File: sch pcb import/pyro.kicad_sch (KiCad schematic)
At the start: 34 parts, among them J601 Screw_01x02, J602 Screw_01x02, Q601 SISA12ADN, Q602 SISA12ADN, U601 LM358, U602 LM358

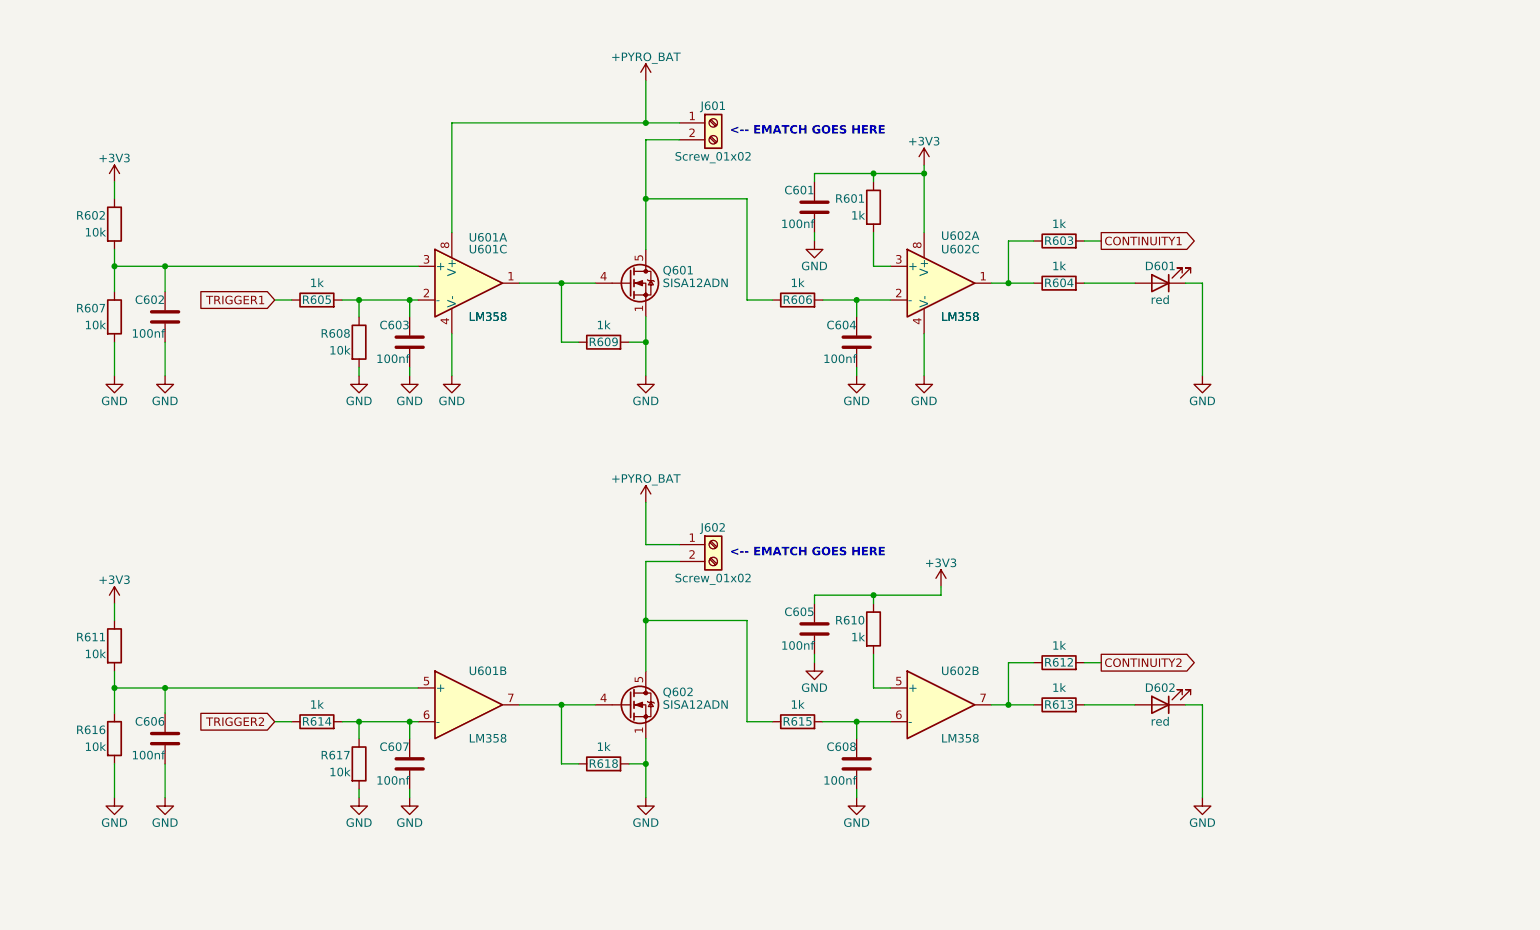
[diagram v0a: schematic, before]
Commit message: added servo and finished esp32 connections
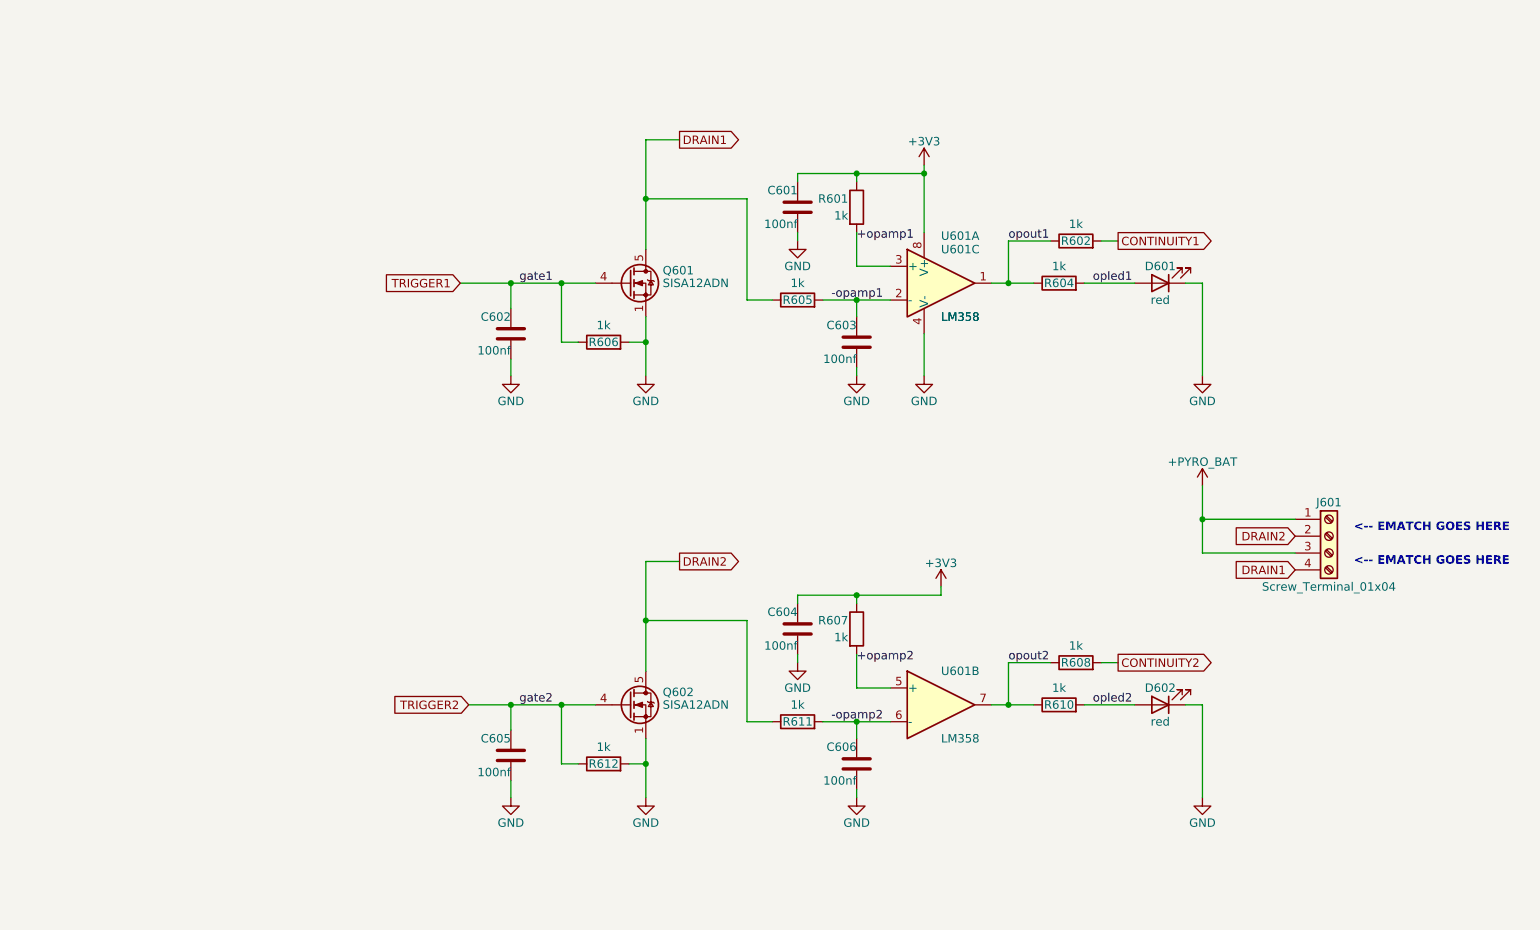
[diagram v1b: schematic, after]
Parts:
- removed C602, C606: 100nf, symbol Device:C
- removed J601, J602: Screw_01x02, symbol Connector:Screw_Terminal_01x02
- removed R602, R607, R608, R611, R616, R617: 10k, symbol Device:R
- removed R605, R614: 1k, symbol Device:R
- removed U601: LM358, Package_SO:SOIC-8_3.9x4.9mm_P1.27mm, symbol Amplifier_Operational:LM358
- added J601: Screw_Terminal_01x04, TerminalBlock:TerminalBlock_Xinya_XY308-2.54-4P_1x04_P2.54mm_Horizontal, symbol Connector:Screw_Terminal_01x04
- renumbered C603 to C602, C604 to C603, C605 to C604, C607 to C605, C608 to C606, R603 to R602, R606 to R605, R609 to R606, R610 to R607, R612 to R608, R613 to R610, R615 to R611, R618 to R612, U602 to U601
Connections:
- net +PYRO_BAT: now also J601.1 (Pin_1), J601.3 (Pin_3)
- net TRIGGER1: now also C602.1, Q601.4 (G), R606.1
- net TRIGGER2: now also C605.1, Q602.4 (G), R612.1
- net opout2: now reaches R608.1, R610.1, U601.7
- net opout1: now reaches R602.1, R604.1, U601.1
- net opled1: now reaches D601.2 (A), R604.2
- net DRAIN1: now reaches Q601.5 (D), R605.1
- net DRAIN1: now also J601.4 (Pin_4)
- net +opamp2: now reaches R607.2, U601.5 (+)
- net DRAIN2: now reaches Q602.5 (D), R611.1
- net DRAIN2: now also J601.2 (Pin_2)
- net -opamp2: now reaches C606.1, R611.2, U601.6 (-)
- net -opamp1: now reaches C603.1, R605.2, U601.2 (-)
- net opled2: now reaches D602.2 (A), R610.2
- net +opamp1: now reaches R601.2, U601.3 (+)
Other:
- company: Done by :- Arudhran -> Drawn by :- Arudhran
- title: AVIONICS PCB -> VECTRON
- moved on the sheet: C601, C602, C604, C605, R601, R602, R607, R608

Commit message: rearranging for aesthetics
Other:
- note added: "E-MATCH SCREW TERMINALS"
- note added: "PYRO-1"
- note added: "PYRO-2"
- moved on the sheet: C601, C602, C603, C604, C605, C606, D601, D602, J601, Q601, Q602, R601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

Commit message: minor changes
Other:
- title: VECTRON -> VECTRON-V1
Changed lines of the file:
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@@
 	(paper "A4")
 	(title_block
-		(title "VECTRON")
-		(date "2025-06-10")
+		(title "VECTRON-V1")
+		(date "2025-06-13")
 		(rev "1.0.0")
 		(company "Drawn by :- Arudhran")

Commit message: minor changes
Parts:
- C601, C602, C603, C604, C605, C606: footprint (none) -> Capacitor_SMD:C_0603_1608Metric
- D601, D602: footprint (none) -> LED_SMD:LED_0603_1608Metric
- R601, R602, R604, R605, R606, R607, R608, R610, R611, R612: footprint (none) -> Resistor_SMD:R_0603_1608Metric
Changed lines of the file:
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@@
 			)
 		)
-		(property "Footprint" ""
+		(property "Footprint" "Resistor_SMD:R_0603_1608Metric"
 			(at 119.38 85.598 90)
 			(effects
@@
 			)
 		)
-		(property "Footprint" ""
+		(property "Footprint" "Capacitor_SMD:C_0603_1608Metric"
 			(at 35.2552 101.6 0)
 			(effects
@@
 			)
 		)
-		(property "Footprint" ""
+		(property "Footprint" "Resistor_SMD:R_0603_1608Metric"
 			(at 116.84 39.878 90)
 			(effects
@@
 			)
 		)
-		(property "Footprint" ""
+		(property "Footprint" "Resistor_SMD:R_0603_1608Metric"
 			(at 84.582 78.74 90)
 			(effects
@@
 			)
 		)
-		(property "Footprint" ""
+		(property "Footprint" "Resistor_SMD:R_0603_1608Metric"
 			(at 48.26 48.768 90)
 			(effects
@@
 			)
 		)
-		(property "Footprint" ""
+		(property "Footprint" "LED_SMD:LED_0603_1608Metric"
 			(at 132.08 38.1 0)
 			(effects
@@
 			)
 		)
-		(property "Footprint" ""
+		(property "Footprint" "Resistor_SMD:R_0603_1608Metric"
 			(at 119.38 33.528 90)
 			(effects
@@
 			)
 		)
-		(property "Footprint" ""
+		(property "Footprint" "Capacitor_SMD:C_0603_1608Metric"
 			(at 87.3252 50.8 0)
 			(effects
@@
 			)
 		)
-		(property "Footprint" ""
+		(property "Footprint" "Resistor_SMD:R_0603_1608Metric"
 			(at 77.47 42.418 90)
 			(effects
@@
 			)
 		)
-		(property "Footprint" ""
+		(property "Footprint" "Resistor_SMD:R_0603_1608Metric"
 			(at 77.47 94.488 90)
 			(effects
@@
 			)
 		)
-		(property "Footprint" ""
+		(property "Footprint" "Resistor_SMD:R_0603_1608Metric"
 			(at 116.84 91.948 90)
 			(effects
@@
 			)
 		)
-		(property "Footprint" ""
+		(property "Footprint" "Capacitor_SMD:C_0603_1608Metric"
 			(at 35.2552 49.53 0)
 			(effects
@@
 			)
 		)
-		(property "Footprint" ""
+		(property "Footprint" "Resistor_SMD:R_0603_1608Metric"
 			(at 48.26 100.838 90)
 			(effects
@@
 			)
 		)
-		(property "Footprint" ""
+		(property "Footprint" "Resistor_SMD:R_0603_1608Metric"
 			(at 84.582 26.67 90)
 			(effects
@@
 			)
 		)
-		(property "Footprint" ""
+		(property "Footprint" "LED_SMD:LED_0603_1608Metric"
 			(at 132.08 90.17 0)
 			(effects
@@
 			)
 		)
-		(property "Footprint" ""
+		(property "Footprint" "Capacitor_SMD:C_0603_1608Metric"
 			(at 78.4352 30.48 0)
 			(effects
@@
 			)
 		)
-		(property "Footprint" ""
+		(property "Footprint" "Capacitor_SMD:C_0603_1608Metric"
 			(at 87.3252 102.87 0)
 			(effects
@@
 			)
 		)
-		(property "Footprint" ""
+		(property "Footprint" "Capacitor_SMD:C_0603_1608Metric"
 			(at 78.4352 82.55 0)
 			(effects

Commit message: minor changes
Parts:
- renumbered R604 to R603, R605 to R604, R606 to R605, R607 to R606, R608 to R607, R610 to R608, R611 to R609, R612 to R610
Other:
- moved on the sheet: C606
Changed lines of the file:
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@@
 	)
 	(junction
-		(at 86.36 92.71)
-		(diameter 0)
-		(color 0 0 0 0)
-	)
-	(junction
 		(at 20.32 129.54)
 		(diameter 0)
@@
 	)
 	(junction
+		(at 85.09 92.71)
+		(diameter 0)
+		(color 0 0 0 0)
+	)
+	(junction
 		(at 54.61 99.06)
 		(diameter 0)
@@
 	(wire
 		(pts
-			(xy 86.36 104.14) (xy 86.36 102.87)
-		)
-		(stroke
-			(width 0)
-			(type default)
-		)
-	)
-	(wire
-		(pts
 			(xy 34.29 38.1) (xy 34.29 41.91)
 		)
@@
 	(wire
 		(pts
-			(xy 86.36 92.71) (xy 86.36 95.25)
-		)
-		(stroke
-			(width 0)
-			(type default)
-		)
-	)
-	(wire
-		(pts
-			(xy 86.36 92.71) (xy 91.44 92.71)
+			(xy 85.09 92.71) (xy 85.09 96.52)
 		)
 		(stroke
@@
 	(wire
 		(pts
+			(xy 85.09 104.14) (xy 85.09 105.41)
+		)
+		(stroke
+			(width 0)
+			(type default)
+		)
+	)
+	(wire
+		(pts
 			(xy 86.36 40.64) (xy 91.44 40.64)
 		)
@@
 	(wire
 		(pts
+			(xy 85.09 92.71) (xy 91.44 92.71)
+		)
+		(stroke
+			(width 0)
+			(type default)
+		)
+	)
+	(wire
+		(pts
 			(xy 109.22 31.75) (xy 115.57 31.75)
 		)
@@
 	(wire
 		(pts
-			(xy 81.28 92.71) (xy 86.36 92.71)
+			(xy 81.28 92.71) (xy 85.09 92.71)
 		)
 		(stroke
@@
 		(on_board yes)
 		(dnp no)
-		(property "Reference" "R608"
+		(property "Reference" "R607"
 			(at 119.38 83.82 90)
 			(effects
@@
 			(project "avionics PCB"
 				(path "/b25900d5-7cd1-4497-821f-c15efd65d19e/d419c042-2463-41ab-9a46-dcddae612d3c"
-					(reference "R608")
+					(reference "R607")
 					(unit 1)
 				)
@@
 		(on_board yes)
 		(dnp no)
-		(property "Reference" "R604"
+		(property "Reference" "R603"
 			(at 116.84 38.1 90)
 			(effects
@@
 			(project "avionics PCB"
 				(path "/b25900d5-7cd1-4497-821f-c15efd65d19e/d419c042-2463-41ab-9a46-dcddae612d3c"
-					(reference "R604")
+					(reference "R603")
 					(unit 1)
 				)
@@
 		(on_board yes)
 		(dnp no)
-		(property "Reference" "R607"
+		(property "Reference" "R606"
 			(at 85.09 77.47 0)
 			(effects
@@
 			(project "avionics PCB"
 				(path "/b25900d5-7cd1-4497-821f-c15efd65d19e/d419c042-2463-41ab-9a46-dcddae612d3c"
-					(reference "R607")
+					(reference "R606")
 					(unit 1)
 				)
@@
 		(on_board yes)
 		(dnp no)
-		(property "Reference" "R606"
+		(property "Reference" "R605"
 			(at 48.26 46.99 90)
 			(effects
@@
 			(project "avionics PCB"
 				(path "/b25900d5-7cd1-4497-821f-c15efd65d19e/d419c042-2463-41ab-9a46-dcddae612d3c"
-					(reference "R606")
+					(reference "R605")
 					(unit 1)
 				)
@@
 		(on_board yes)
 		(dnp no)
-		(property "Reference" "#PWR0602"
+		(property "Reference" "#PWR0601"
 			(at 96.52 24.13 0)
 			(effects
@@
 			(project ""
 				(path "/b25900d5-7cd1-4497-821f-c15efd65d19e/d419c042-2463-41ab-9a46-dcddae612d3c"
-					(reference "#PWR0602")
+					(reference "#PWR0601")
 					(unit 1)
 				)
@@
 		(on_board yes)
 		(dnp no)
-		(property "Reference" "#PWR0612"
+		(property "Reference" "#PWR0610"
 			(at 34.29 110.49 0)
 			(effects
@@
 			(project "avionics PCB"
 				(path "/b25900d5-7cd1-4497-821f-c15efd65d19e/d419c042-2463-41ab-9a46-dcddae612d3c"
-					(reference "#PWR0612")
+					(reference "#PWR0610")
 					(unit 1)
 				)
@@
 		(on_board yes)
 		(dnp no)
-		(property "Reference" "#PWR0605"
+		(property "Reference" "#PWR0604"
 			(at 54.61 58.42 0)
 			(effects
@@
 			(project ""
 				(path "/b25900d5-7cd1-4497-821f-c15efd65d19e/d419c042-2463-41ab-9a46-dcddae612d3c"
-					(reference "#PWR0605")
+					(reference "#PWR0604")
 					(unit 1)
 				)
@@
 		(on_board yes)
 		(dnp no)
-		(property "Reference" "#PWR0608"
+		(property "Reference" "#PWR0607"
 			(at 138.43 58.42 0)
 			(effects
@@
 			(project "avionics PCB"
 				(path "/b25900d5-7cd1-4497-821f-c15efd65d19e/d419c042-2463-41ab-9a46-dcddae612d3c"
-					(reference "#PWR0608")
+					(reference "#PWR0607")
 					(unit 1)
 				)
@@
 		(on_board yes)
 		(dnp no)
-		(property "Reference" "#PWR0615"
+		(property "Reference" "#PWR0612"
 			(at 138.43 110.49 0)
 			(effects
@@
 			(project "avionics PCB"
 				(path "/b25900d5-7cd1-4497-821f-c15efd65d19e/d419c042-2463-41ab-9a46-dcddae612d3c"
-					(reference "#PWR0615")
+					(reference "#PWR0612")
 					(unit 1)
 				)
@@
 		(on_board yes)
 		(dnp no)
-		(property "Reference" "R605"
+		(property "Reference" "R604"
 			(at 77.47 40.64 90)
 			(effects
@@
 			(project "avionics PCB"
 				(path "/b25900d5-7cd1-4497-821f-c15efd65d19e/d419c042-2463-41ab-9a46-dcddae612d3c"
-					(reference "R605")
+					(reference "R604")
 					(unit 1)
 				)
@@
 		(on_board yes)
 		(dnp no)
-		(property "Reference" "R611"
+		(property "Reference" "R609"
 			(at 77.47 92.71 90)
 			(effects
@@
 			(project "avionics PCB"
 				(path "/b25900d5-7cd1-4497-821f-c15efd65d19e/d419c042-2463-41ab-9a46-dcddae612d3c"
-					(reference "R611")
+					(reference "R609")
 					(unit 1)
 				)
@@
 		(on_board yes)
 		(dnp no)
-		(property "Reference" "R610"
+		(property "Reference" "R608"
 			(at 116.84 90.17 90)
 			(effects
@@
 			(project "avionics PCB"
 				(path "/b25900d5-7cd1-4497-821f-c15efd65d19e/d419c042-2463-41ab-9a46-dcddae612d3c"
-					(reference "R610")
+					(reference "R608")
 					(unit 1)
 				)
@@
 	(symbol
 		(lib_id "power:GND")
-		(at 86.36 104.14 0)
+		(at 85.09 105.41 0)
 		(unit 1)
 		(exclude_from_sim no)
@@
 		(on_board yes)
 		(dnp no)
-		(property "Reference" "#PWR0614"
-			(at 86.36 110.49 0)
+		(property "Reference" "#PWR0613"
+			(at 85.09 111.76 0)
 			(effects
 				(font
@@
 		)
 		(property "Value" "GND"
-			(at 86.36 107.95 0)
+			(at 85.09 109.22 0)
 			(effects
 				(font
@@
 		)
 		(property "Footprint" ""
-			(at 86.36 104.14 0)
+			(at 85.09 105.41 0)
 			(effects
 				(font
@@
 		)
 		(property "Datasheet" ""
-			(at 86.36 104.14 0)
+			(at 85.09 105.41 0)
 			(effects
 				(font
@@
 		)
 		(property "Description" "Power symbol creates a global label with name \"GND\" , ground"
-			(at 86.36 104.14 0)
+			(at 85.09 105.41 0)
 			(effects
 				(font
@@
 			(project "avionics PCB"
 				(path "/b25900d5-7cd1-4497-821f-c15efd65d19e/d419c042-2463-41ab-9a46-dcddae612d3c"
-					(reference "#PWR0614")
+					(reference "#PWR0613")
 					(unit 1)
 				)
@@
 		(on_board yes)
 		(dnp no)
-		(property "Reference" "#PWR0607"
+		(property "Reference" "#PWR0606"
 			(at 96.52 58.42 0)
 			(effects
@@
 			(project "avionics PCB"
 				(path "/b25900d5-7cd1-4497-821f-c15efd65d19e/d419c042-2463-41ab-9a46-dcddae612d3c"
-					(reference "#PWR0607")
+					(reference "#PWR0606")
 					(unit 1)
 				)
@@
 		(on_board yes)
 		(dnp no)
-		(property "Reference" "#PWR0613"
+		(property "Reference" "#PWR0611"
 			(at 54.61 110.49 0)
 			(effects
@@
 			(project "avionics PCB"
 				(path "/b25900d5-7cd1-4497-821f-c15efd65d19e/d419c042-2463-41ab-9a46-dcddae612d3c"
-					(reference "#PWR0613")
+					(reference "#PWR0611")
 					(unit 1)
 				)
@@
 		(on_board yes)
 		(dnp no)
-		(property "Reference" "R612"
+		(property "Reference" "R610"
 			(at 48.26 99.06 90)
 			(effects
@@
 			(project "avionics PCB"
 				(path "/b25900d5-7cd1-4497-821f-c15efd65d19e/d419c042-2463-41ab-9a46-dcddae612d3c"
-					(reference "R612")
+					(reference "R610")
 					(unit 1)
 				)
@@
 		(on_board yes)
 		(dnp no)
-		(property "Reference" "#PWR0610"
+		(property "Reference" "#PWR0608"
 			(at 99.06 76.2 0)
 			(effects
@@
 			(project "avionics PCB"
 				(path "/b25900d5-7cd1-4497-821f-c15efd65d19e/d419c042-2463-41ab-9a46-dcddae612d3c"
-					(reference "#PWR0610")
+					(reference "#PWR0608")
 					(unit 1)
 				)
@@
 		(on_board yes)
 		(dnp no)
-		(property "Reference" "#PWR0606"
+		(property "Reference" "#PWR0605"
 			(at 86.36 58.42 0)
 			(effects
@@
 			(project "avionics PCB"
 				(path "/b25900d5-7cd1-4497-821f-c15efd65d19e/d419c042-2463-41ab-9a46-dcddae612d3c"
-					(reference "#PWR0606")
+					(reference "#PWR0605")
 					(unit 1)
 				)
@@
 		(on_board yes)
 		(dnp no)
-		(property "Reference" "#PWR0603"
+		(property "Reference" "#PWR0602"
 			(at 77.47 38.1 0)
 			(effects
@@
 			(project "avionics PCB"
 				(path "/b25900d5-7cd1-4497-821f-c15efd65d19e/d419c042-2463-41ab-9a46-dcddae612d3c"
-					(reference "#PWR0603")
+					(reference "#PWR0602")
 					(unit 1)
 				)
@@
 		(on_board yes)
 		(dnp no)
-		(property "Reference" "#PWR0611"
+		(property "Reference" "#PWR0609"
 			(at 77.47 90.17 0)
 			(effects
@@
 			(project "avionics PCB"
 				(path "/b25900d5-7cd1-4497-821f-c15efd65d19e/d419c042-2463-41ab-9a46-dcddae612d3c"
-					(reference "#PWR0611")
+					(reference "#PWR0609")
 					(unit 1)
 				)
@@
 	(symbol
 		(lib_id "Device:C")
-		(at 86.36 99.06 0)
+		(at 85.09 100.33 0)
 		(unit 1)
 		(exclude_from_sim no)
@@
 		(dnp no)
 		(property "Reference" "C606"
-			(at 86.36 96.52 0)
+			(at 85.09 97.79 0)
 			(effects
 				(font
@@
 		)
 		(property "Value" "100nf"
-			(at 86.36 101.6 0)
+			(at 85.09 102.87 0)
 			(effects
 				(font
@@
 		)
 		(property "Footprint" "Capacitor_SMD:C_0603_1608Metric"
-			(at 87.3252 102.87 0)
+			(at 86.0552 104.14 0)
 			(effects
 				(font
@@
 		)
 		(property "Datasheet" "~"
-			(at 86.36 99.06 0)
+			(at 85.09 100.33 0)
 			(effects
 				(font
@@
 		)
 		(property "Description" "Unpolarized capacitor"
-			(at 86.36 99.06 0)
+			(at 85.09 100.33 0)
 			(effects
 				(font
@@
 		(on_board yes)
 		(dnp no)
-		(property "Reference" "#PWR0604"
+		(property "Reference" "#PWR0603"
 			(at 34.29 58.42 0)
 			(effects
@@
 			(project "avionics PCB"
 				(path "/b25900d5-7cd1-4497-821f-c15efd65d19e/d419c042-2463-41ab-9a46-dcddae612d3c"
-					(reference "#PWR0604")
+					(reference "#PWR0603")
 					(unit 1)
 				)
@@
 		(on_board yes)
 		(dnp no)
-		(property "Reference" "#PWR0601"
+		(property "Reference" "#PWR0614"
 			(at 20.32 128.27 0)
 			(effects
@@
 			(project "vectron"
 				(path "/b25900d5-7cd1-4497-821f-c15efd65d19e/d419c042-2463-41ab-9a46-dcddae612d3c"
-					(reference "#PWR0601")
+					(reference "#PWR0614")
 					(unit 1)
 				)

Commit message: minor changes
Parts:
- added R611, R612: 10k, Resistor_SMD:R_0603_1608Metric, symbol Device:R
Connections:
- net +3V3: now also R601.2, R606.2; no longer C601.1, C604.1, R601.1, R606.1
- net +PYRO_BAT: now also J601.4 (Pin_4); no longer J601.3 (Pin_3)
- net +opamp1: now also C601.1, R601.1, U601.2 (-); no longer R601.2, U601.3 (+)
- net +opamp2: now also C604.1, R606.1, U601.6 (-); no longer R606.2, U601.5 (+)
- net -opamp1: now also U601.3 (+); no longer U601.2 (-)
- net -opamp2: now also U601.5 (+); no longer U601.6 (-)
- net DRAIN1: now also J601.2 (Pin_2), R611.1; no longer J601.4 (Pin_4)
- net DRAIN2: now also J601.3 (Pin_3), R612.1; no longer J601.2 (Pin_2)
- net GND: now also R611.2, R612.2
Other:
- company: Drawn by :- Arudhran -> (none)
